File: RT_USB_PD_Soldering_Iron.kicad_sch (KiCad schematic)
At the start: 61 parts, among them J1 USB4105-GF-A, J2 35RASMT4BHNTRX, J3 Conn_02x03_Odd_Even, SW1 SW_Push, SW2 SW_Push, U1 SPX3819M5-L-3-3, U2 BMI270, U3 ECMF02-AMX6, U4 FUSB302BMPX, U5 STM32G431Kxxx, U6 TPS25982ONRGET, U7 OPA376AIDCKR

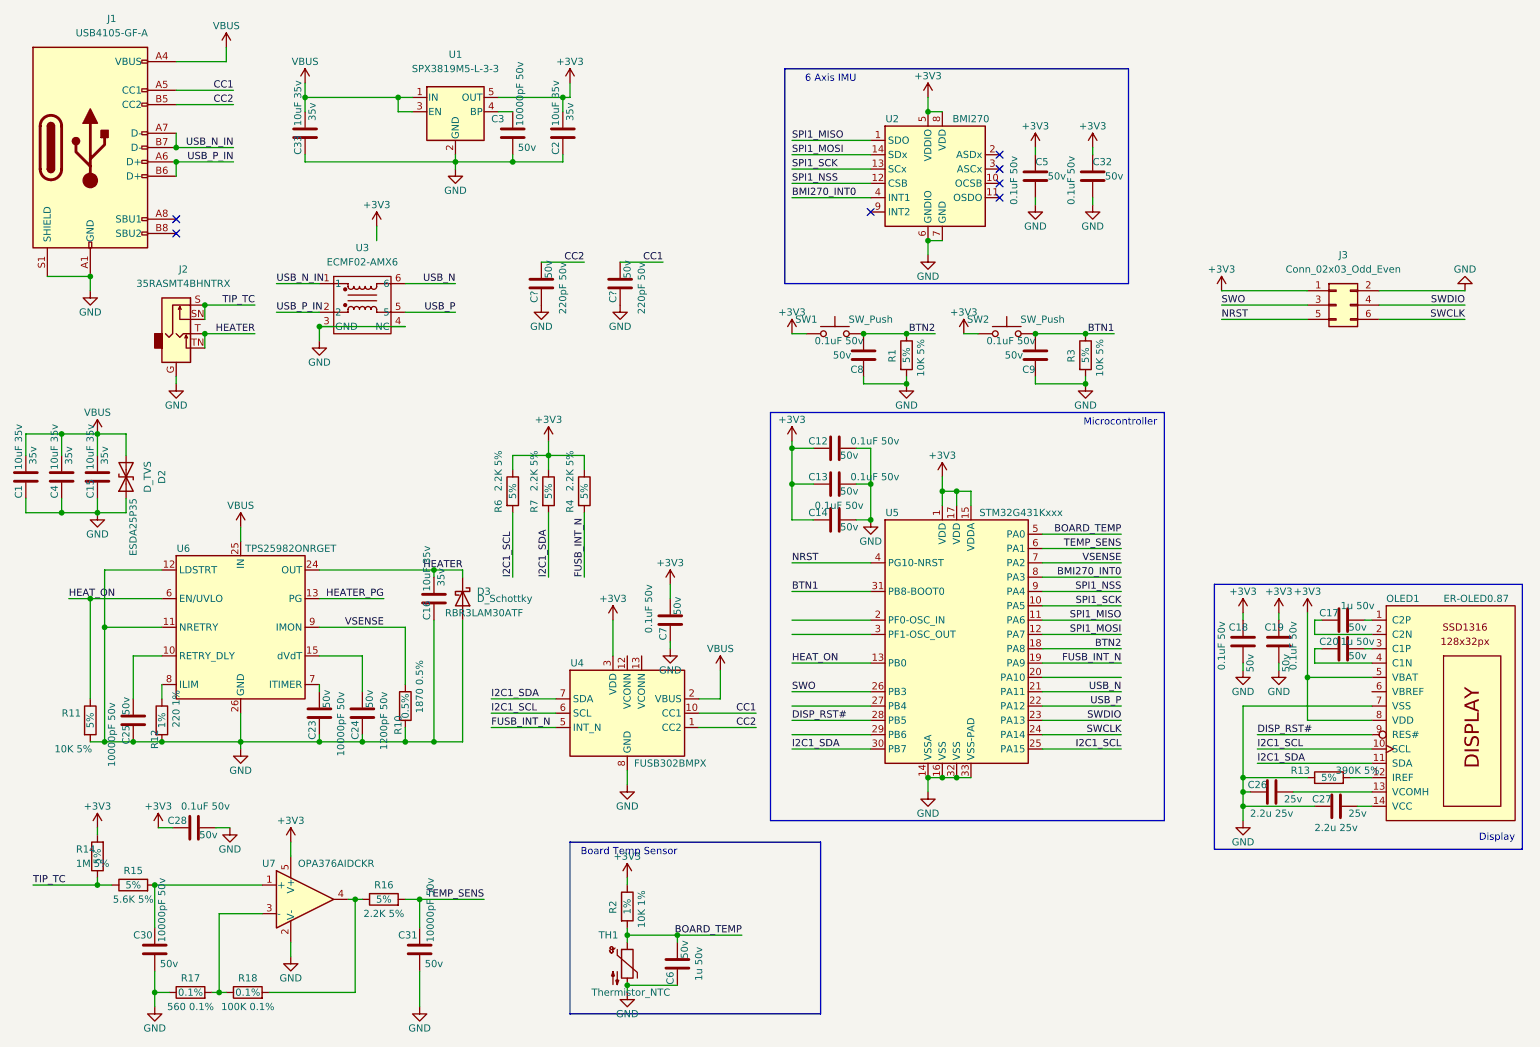
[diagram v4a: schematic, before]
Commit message: Add mounting holes, change diode
added mounting holes and changed the diode to a much smaller part.
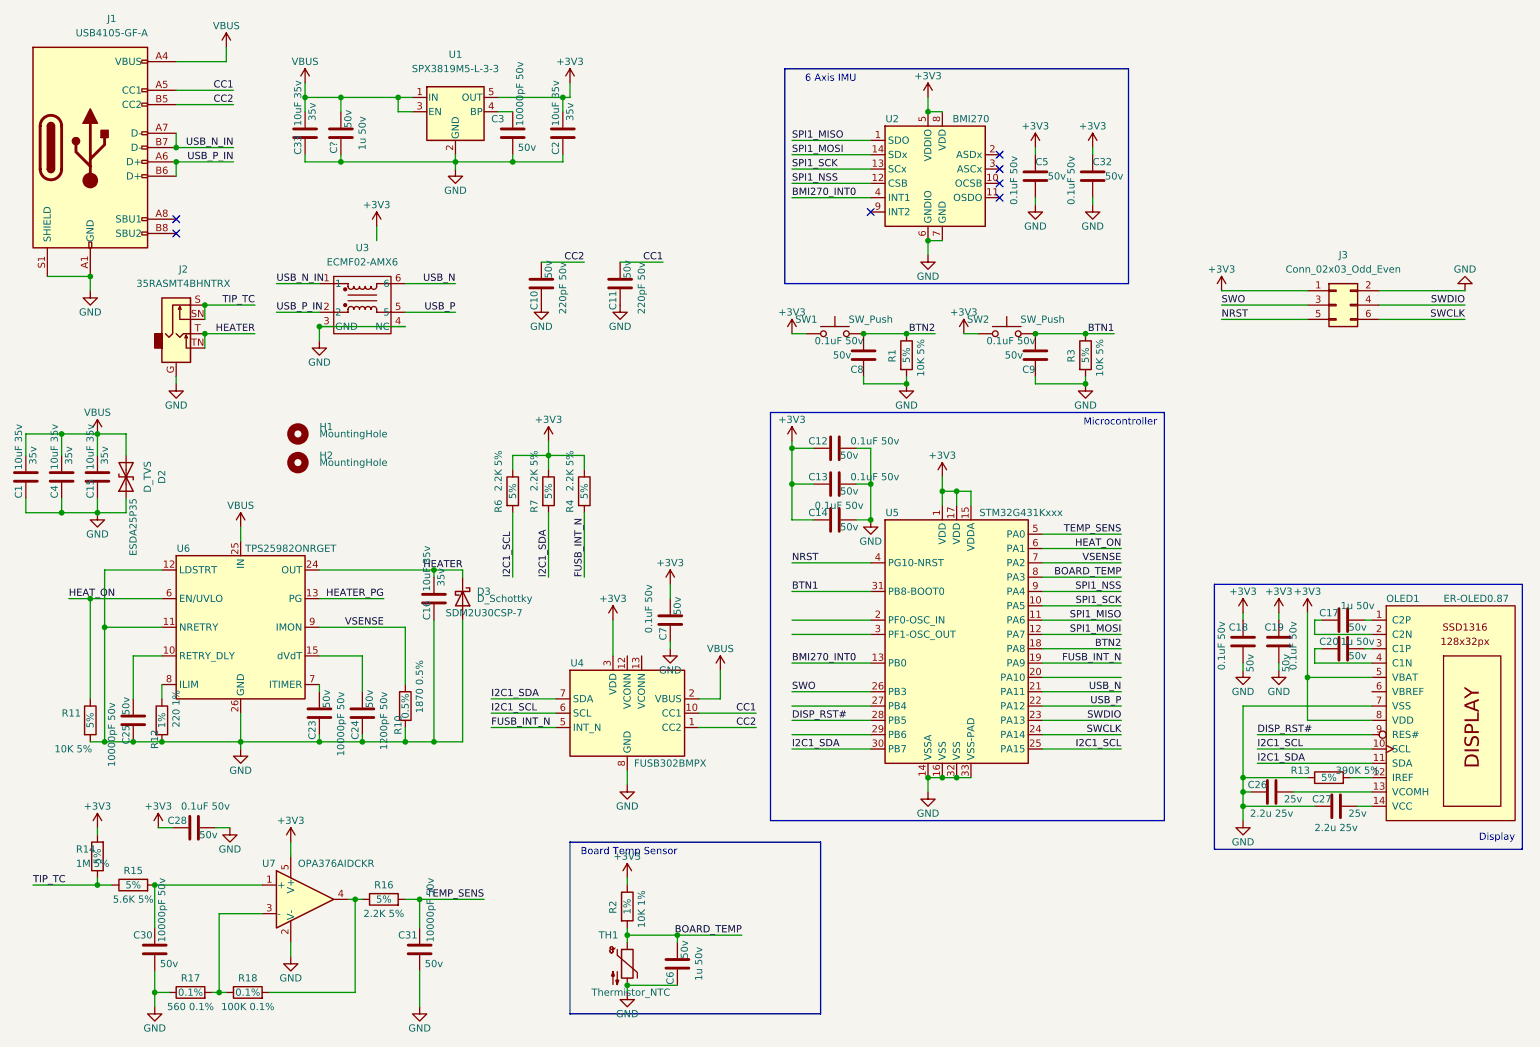
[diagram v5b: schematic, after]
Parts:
- added C?: 1u 50v, Capacitor_SMD:C_0402_1005Metric, symbol Device:C
- added H1, H2: MountingHole, MountingHole:MountingHole_2.2mm_M2_ISO7380, symbol Mechanical:MountingHole
- D3: footprint Diode_SMD:D_SOD-128 -> local:X3-WLB1608-2; Part RBR3LAM30ATF -> SDM2U30CSP-7
- gave numbers to parts that had none: 2
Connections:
- net BMI270_INT0: now also U5.13 (PB0); no longer U5.8 (PA3)
- net BOARD_TEMP: now also U5.8 (PA3); no longer U5.5 (PA0)
- net GND: now also C?.1
- net HEAT_ON: now also U5.6 (PA1); no longer U5.13 (PB0)
- net IN: now also C?.2
- net TEMP_SENS: now also U5.5 (PA0); no longer U5.6 (PA1)
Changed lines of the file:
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@@
   (junction (at 68.58 69.85) (diameter 1.016) (color 0 0 0 0))
   (junction (at 68.58 143.51) (diameter 1.016) (color 0 0 0 0))
+  (junction (at 72.39 29.21) (diameter 1.016) (color 0 0 0 0))
+  (junction (at 72.39 40.64) (diameter 1.016) (color 0 0 0 0))
   (junction (at 74.93 171.45) (diameter 1.016) (color 0 0 0 0))
   (junction (at 76.2 143.51) (diameter 1.016) (color 0 0 0 0))
@@
     (stroke (width 0) (type solid) (color 0 0 0 0))
   )
-  (wire (pts (xy 66.04 29.21) (xy 82.55 29.21))
+  (wire (pts (xy 66.04 29.21) (xy 72.39 29.21))
     (stroke (width 0) (type solid) (color 0 0 0 0))
   )
@@
     (stroke (width 0) (type solid) (color 0 0 0 0))
   )
-  (wire (pts (xy 66.04 40.64) (xy 92.71 40.64))
+  (wire (pts (xy 66.04 40.64) (xy 72.39 40.64))
     (stroke (width 0) (type solid) (color 0 0 0 0))
   )
@@
   )
   (wire (pts (xy 68.58 143.51) (xy 76.2 143.51))
+    (stroke (width 0) (type solid) (color 0 0 0 0))
+  )
+  (wire (pts (xy 72.39 29.21) (xy 72.39 31.75))
+    (stroke (width 0) (type solid) (color 0 0 0 0))
+  )
+  (wire (pts (xy 72.39 29.21) (xy 82.55 29.21))
+    (stroke (width 0) (type solid) (color 0 0 0 0))
+  )
+  (wire (pts (xy 72.39 39.37) (xy 72.39 40.64))
+    (stroke (width 0) (type solid) (color 0 0 0 0))
+  )
+  (wire (pts (xy 72.39 40.64) (xy 92.71 40.64))
     (stroke (width 0) (type solid) (color 0 0 0 0))
   )
@@
     (effects (font (size 1.27 1.27)) (justify left bottom))
   )
-  (label "HEAT_ON" (at 152.4 129.54 0)
+  (label "BMI270_INT0" (at 152.4 129.54 0)
     (effects (font (size 1.27 1.27)) (justify left bottom))
   )
@@
     (effects (font (size 1.27 1.27)) (justify right bottom))
   )
-  (label "BOARD_TEMP" (at 210.82 106.68 180)
-    (effects (font (size 1.27 1.27)) (justify right bottom))
-  )
-  (label "TEMP_SENS" (at 210.82 109.22 180)
+  (label "TEMP_SENS" (at 210.82 106.68 180)
+    (effects (font (size 1.27 1.27)) (justify right bottom))
+  )
+  (label "HEAT_ON" (at 210.82 109.22 180)
     (effects (font (size 1.27 1.27)) (justify right bottom))
   )
@@
     (effects (font (size 1.27 1.27)) (justify right bottom))
   )
-  (label "BMI270_INT0" (at 210.82 114.3 180)
+  (label "BOARD_TEMP" (at 210.82 114.3 180)
     (effects (font (size 1.27 1.27)) (justify right bottom))
   )
@@
   (symbol (lib_id "power:GND") (at 107.95 66.04 0) (unit 1)
     (in_bom yes) (on_board yes)
-    (property "Reference" "#PWR?" (id 0) (at 107.95 72.39 0)
+    (property "Reference" "#PWR0121" (id 0) (at 107.95 72.39 0)
       (effects (font (size 1.27 1.27)) hide)
     )
@@
   (symbol (lib_id "power:GND") (at 121.92 66.04 0) (unit 1)
     (in_bom yes) (on_board yes)
-    (property "Reference" "#PWR?" (id 0) (at 121.92 72.39 0)
+    (property "Reference" "#PWR0131" (id 0) (at 121.92 72.39 0)
       (effects (font (size 1.27 1.27)) hide)
     )
@@
     )
     (property "Datasheet" "" (id 3) (at 271.78 63.5 0)
+      (effects (font (size 1.27 1.27)) hide)
+    )
+  )
+  (symbol (lib_id "Mechanical:MountingHole") (at 64.77 88.9 0) (unit 1)
+    (in_bom yes) (on_board yes)
+    (property "Reference" "H1" (id 0) (at 68.58 87.63 0)
+      (effects (font (size 1.27 1.27)) (justify left))
+    )
+    (property "Value" "MountingHole" (id 1) (at 68.58 88.9 0)
+      (effects (font (size 1.27 1.27)) (justify left))
+    )
+    (property "Footprint" "MountingHole:MountingHole_2.2mm_M2_ISO7380" (id 2) (at 64.77 88.9 0)
+      (effects (font (size 1.27 1.27)) hide)
+    )
+    (property "Datasheet" "~" (id 3) (at 64.77 88.9 0)
+      (effects (font (size 1.27 1.27)) hide)
+    )
+  )
+  (symbol (lib_id "Mechanical:MountingHole") (at 64.77 93.98 0) (unit 1)
+    (in_bom yes) (on_board yes)
+    (property "Reference" "H2" (id 0) (at 68.58 92.71 0)
+      (effects (font (size 1.27 1.27)) (justify left))
+    )
+    (property "Value" "MountingHole" (id 1) (at 68.58 93.98 0)
+      (effects (font (size 1.27 1.27)) (justify left))
+    )
+    (property "Footprint" "MountingHole:MountingHole_2.2mm_M2_ISO7380" (id 2) (at 64.77 93.98 0)
+      (effects (font (size 1.27 1.27)) hide)
+    )
+    (property "Datasheet" "~" (id 3) (at 64.77 93.98 0)
       (effects (font (size 1.27 1.27)) hide)
     )
@@
       (effects (font (size 1.27 1.27)) (justify left))
     )
-    (property "Footprint" "Diode_SMD:D_SOD-128" (id 2) (at 93.98 118.11 0)
+    (property "Footprint" "local:X3-WLB1608-2" (id 2) (at 93.98 118.11 0)
       (effects (font (size 1.27 1.27)) hide)
     )
@@
       (effects (font (size 1.27 1.27)) hide)
     )
-    (property "Part" "RBR3LAM30ATF" (id 4) (at 97.79 120.65 90))
+    (property "Part" "SDM2U30CSP-7" (id 4) (at 97.79 120.65 90))
   )
   (symbol (lib_id "Device:C") (at 16.51 96.52 0) (unit 1)
@@
     (property "Voltage" "50v" (id 4) (at 69.85 135.89 90))
   )
+  (symbol (lib_id "Device:C") (at 72.39 35.56 180) (unit 1)
+    (in_bom yes) (on_board yes)
+    (property "Reference" "C?" (id 0) (at 71.12 38.1 90))
+    (property "Value" "1u 50v" (id 1) (at 76.2 35.56 90))
+    (property "Footprint" "Capacitor_SMD:C_0402_1005Metric" (id 2) (at 71.4248 31.75 0)
+      (effects (font (size 1.27 1.27)) hide)
+    )
+    (property "Datasheet" "~" (id 3) (at 72.39 35.56 0)
+      (effects (font (size 1.27 1.27)) hide)
+    )
+    (property "Voltage" "50v" (id 4) (at 73.66 33.02 90))
+  )
   (symbol (lib_id "Device:C") (at 76.2 138.43 180) (unit 1)
     (in_bom yes) (on_board yes)
@@
   (symbol (lib_id "Device:C") (at 107.95 62.23 180) (unit 1)
     (in_bom yes) (on_board yes)
-    (property "Reference" "C?" (id 0) (at 106.68 63.5 90)
+    (property "Reference" "C10" (id 0) (at 106.68 63.5 90)
       (effects (font (size 1.27 1.27)) (justify left))
     )
@@
   (symbol (lib_id "Device:C") (at 121.92 62.23 180) (unit 1)
     (in_bom yes) (on_board yes)
-    (property "Reference" "C?" (id 0) (at 120.65 63.5 90)
+    (property "Reference" "C11" (id 0) (at 120.65 63.5 90)
       (effects (font (size 1.27 1.27)) (justify left))
     )
@@
       (reference "#PWR0120") (unit 1) (value "GND") (footprint "")
     )
+    (path "/e09f0c59-3c93-4508-9255-853445ccd567"
+      (reference "#PWR0121") (unit 1) (value "GND") (footprint "")
+    )
     (path "/ebdd60b3-746b-441c-b97d-ee98cfb54686"
       (reference "#PWR0122") (unit 1) (value "VBUS") (footprint "")
@@
       (reference "#PWR0130") (unit 1) (value "GND") (footprint "")
     )
+    (path "/ee20b851-f190-40ff-8552-07d58396d6eb"
+      (reference "#PWR0131") (unit 1) (value "GND") (footprint "")
+    )
     (path "/476b625b-6a95-489c-9b91-ca924a16530f"
       (reference "#PWR0133") (unit 1) (value "GND") (footprint "")
@@
       (reference "#PWR0151") (unit 1) (value "+3V3") (footprint "")
     )
-    (path "/e09f0c59-3c93-4508-9255-853445ccd567"
-      (reference "#PWR?") (unit 1) (value "GND") (footprint "")
-    )
-    (path "/ee20b851-f190-40ff-8552-07d58396d6eb"
-      (reference "#PWR?") (unit 1) (value "GND") (footprint "")
-    )
     (path "/c98d6c66-4473-4c20-8c07-ea6fc2312536"
       (reference "C1") (unit 1) (value "10uF 35v") (footprint "Capacitor_SMD:C_0603_1608Metric_Pad1.05x0.95mm_HandSolder")
@@
       (reference "C9") (unit 1) (value "0.1uF 50v") (footprint "Capacitor_SMD:C_0402_1005Metric")
     )
+    (path "/1cf02831-66df-474e-bb22-5dba0f0b0919"
+      (reference "C10") (unit 1) (value "220pF 50v") (footprint "Capacitor_SMD:C_0402_1005Metric")
+    )
+    (path "/a6b69c27-dbcc-4ea3-b742-20ccee9cf778"
+      (reference "C11") (unit 1) (value "220pF 50v") (footprint "Capacitor_SMD:C_0402_1005Metric")
+    )
     (path "/c419ceab-1e68-4be9-8723-76ea54574acf"
       (reference "C12") (unit 1) (value "0.1uF 50v") (footprint "Capacitor_SMD:C_0402_1005Metric")
@@
       (reference "C33") (unit 1) (value "10uF 35v") (footprint "Capacitor_SMD:C_0603_1608Metric_Pad1.05x0.95mm_HandSolder")
     )
-    (path "/1cf02831-66df-474e-bb22-5dba0f0b0919"
-      (reference "C?") (unit 1) (value "220pF 50v") (footprint "Capacitor_SMD:C_0402_1005Metric")
-    )
-    (path "/a6b69c27-dbcc-4ea3-b742-20ccee9cf778"
-      (reference "C?") (unit 1) (value "220pF 50v") (footprint "Capacitor_SMD:C_0402_1005Metric")
+    (path "/86e9954a-b266-4cc6-8219-d1adb3bf7083"
+      (reference "C?") (unit 1) (value "1u 50v") (footprint "Capacitor_SMD:C_0402_1005Metric")
     )
     (path "/930b46a1-bcfa-4351-bda0-12fa566d3580"
@@
     )
     (path "/df2137d6-6a3e-4b97-ae34-985653b3111b"
-      (reference "D3") (unit 1) (value "D_Schottky") (footprint "Diode_SMD:D_SOD-128")
+      (reference "D3") (unit 1) (value "D_Schottky") (footprint "local:X3-WLB1608-2")
+    )
+    (path "/ffc9b8c7-d039-4169-9ffd-a8a17d23ff13"
+      (reference "H1") (unit 1) (value "MountingHole") (footprint "MountingHole:MountingHole_2.2mm_M2_ISO7380")
+    )
+    (path "/54ec1b8d-8ea6-48ad-b832-ec785bd67a48"
+      (reference "H2") (unit 1) (value "MountingHole") (footprint "MountingHole:MountingHole_2.2mm_M2_ISO7380")
     )
     (path "/a9b433d3-f6a8-447d-add7-160962cdce04"

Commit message: Power trace changes, pin changes
updated the power traces for better current return path. Connected PG from the high side switch.
Lots of pin changes for better layout.
re-annotated schematic
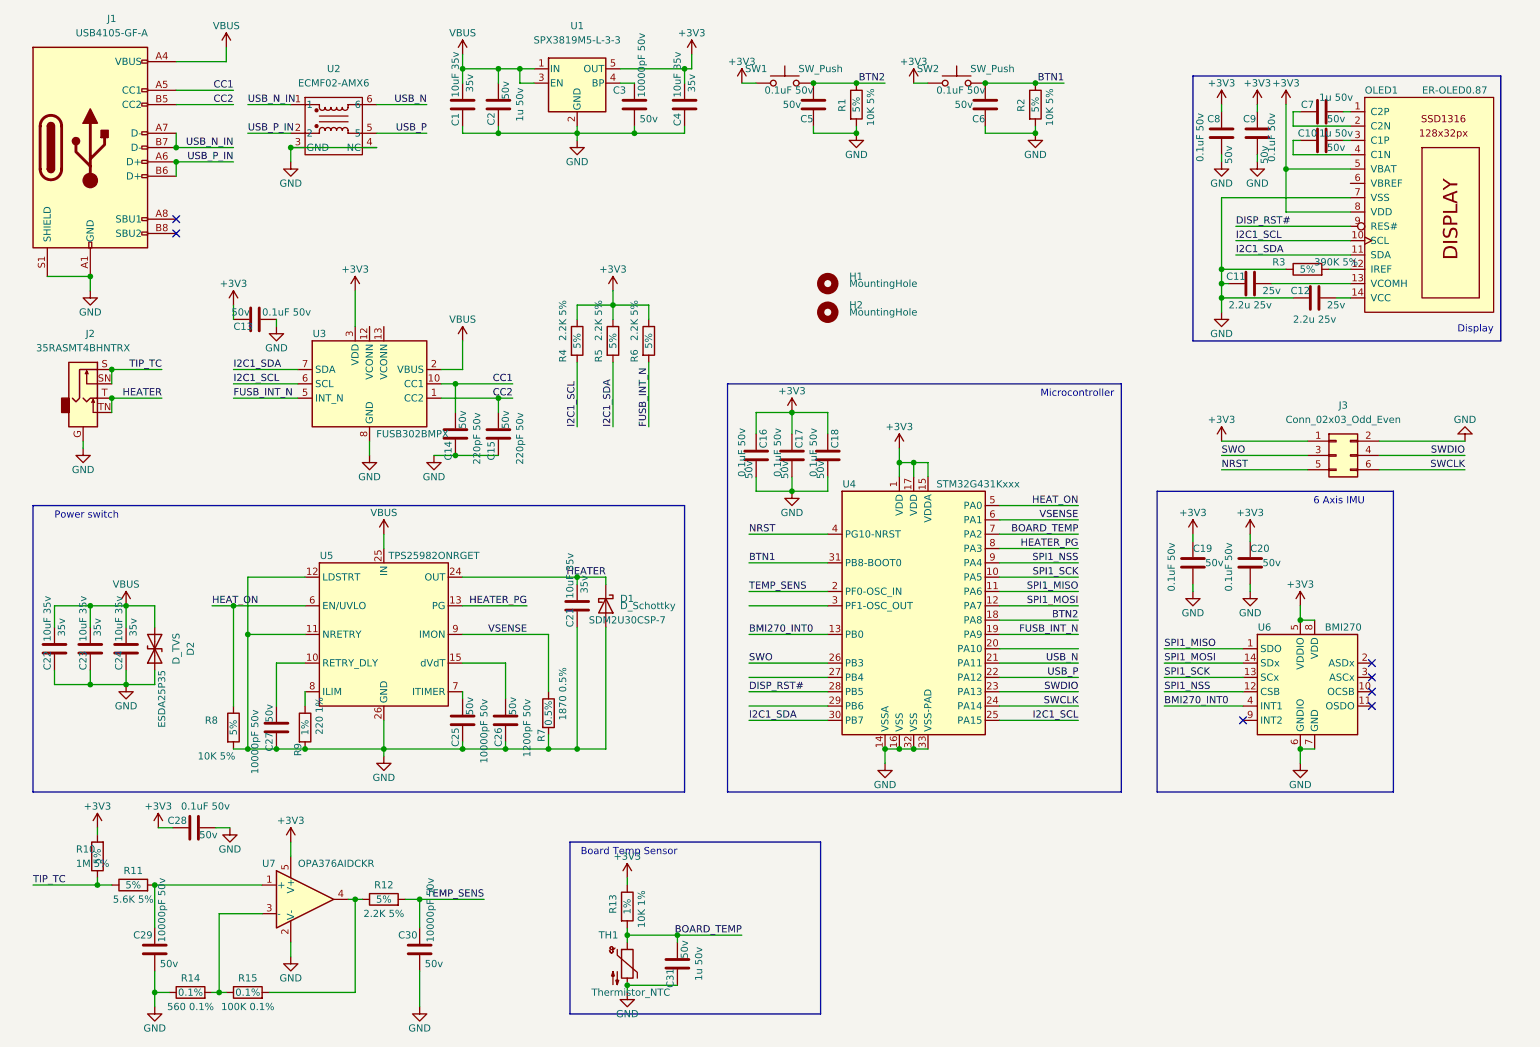
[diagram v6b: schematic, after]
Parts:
- gave numbers to parts that had none: 1
- renumbered C33 to C1, C20 to C10, C26 to C11, C27 to C12, C7 to C13, C11 to C14, C10 to C15, C14 to C16, C13 to C17, C12 to C18, C5 to C19, C32 to C20, C16 to C21, C1 to C22, C4 to C23, C15 to C24, C23 to C25, C24 to C26, C25 to C27, C30 to C29, C31 to C30, C6 to C31, C2 to C4, C8 to C5, C9 to C6, C17 to C7, C18 to C8, C19 to C9, D3 to D1, R14 to R10, R15 to R11, R16 to R12, R2 to R13, R17 to R14, R18 to R15, R3 to R2, R13 to R3, R6 to R4, R7 to R5, R4 to R6, R10 to R7, R11 to R8, R12 to R9, U3 to U2, U4 to U3, U5 to U4, U6 to U5, U2 to U6
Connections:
- net BOARD_TEMP: now also U4.7 (PA2); no longer U4.8 (PA3)
- net HEATER_PG: now also U4.8 (PA3)
- net HEAT_ON: now also U4.5 (PA0); no longer U4.6 (PA1)
- net TEMP_SENS: now also U4.2 (PF0-OSC_IN); no longer U4.5 (PA0)
- net VSENSE: now also U4.6 (PA1); no longer U4.7 (PA2)
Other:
- note added: "Power switch"
- moved on the sheet: C1, C10, C11, C12, C13, C14, C15, C16, C17, C18, C19, C2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
